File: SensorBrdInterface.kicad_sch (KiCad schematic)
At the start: 15 parts

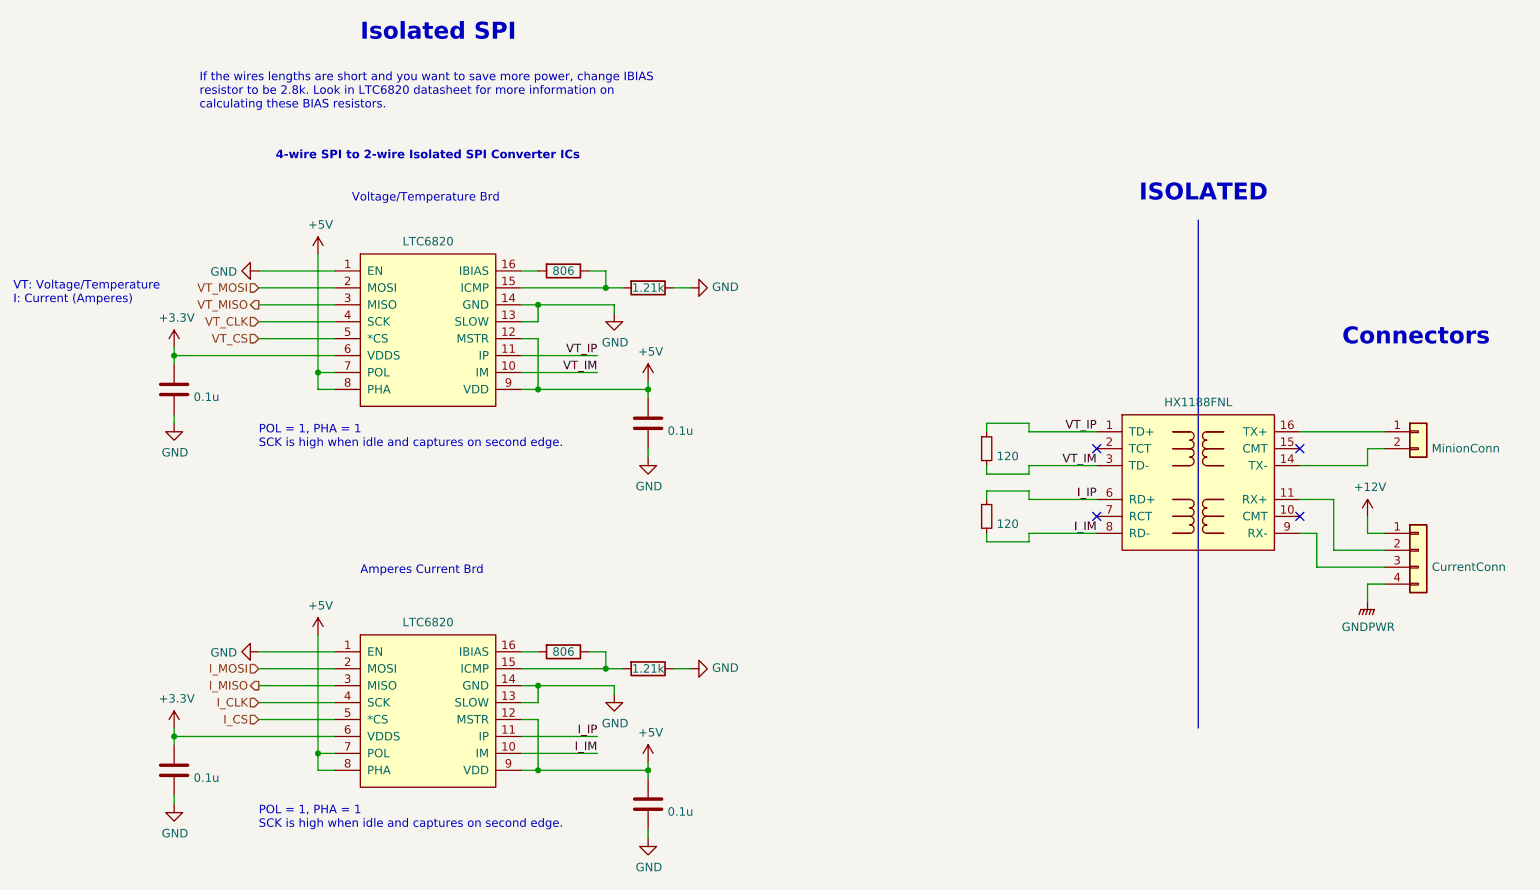
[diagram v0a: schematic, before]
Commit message: Update repo to only use one common library
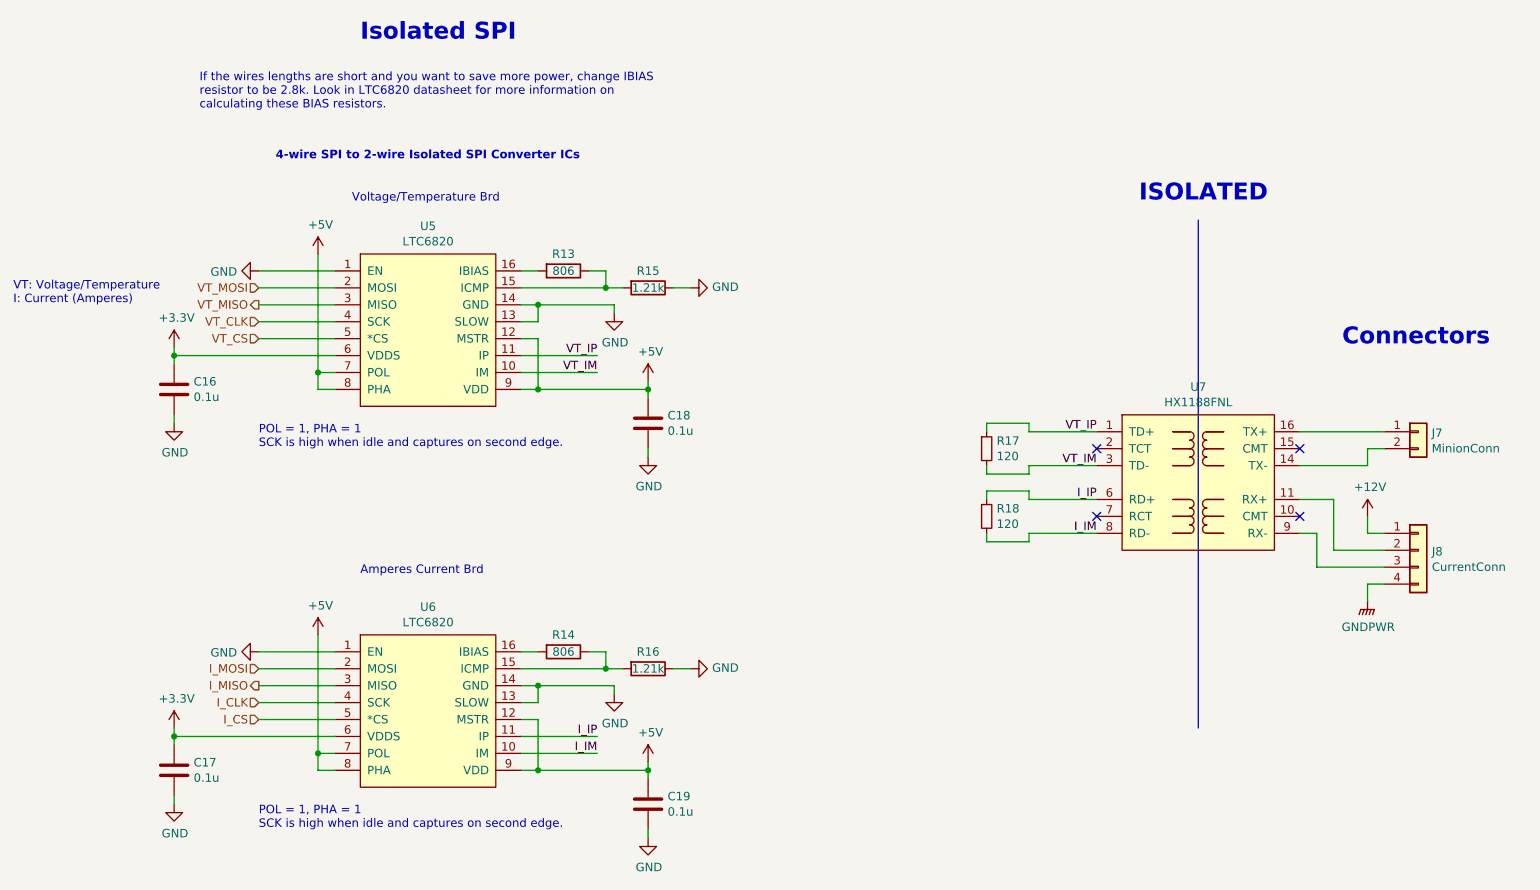
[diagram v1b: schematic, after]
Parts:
- gave numbers to parts that had none: 15
